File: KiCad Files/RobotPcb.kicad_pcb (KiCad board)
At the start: 2 copper layers, 68.8 x 98.6 mm, 35 parts, among them IC1 LM2576, IC2 LM2576, IC3 L293D, IC4 L293D, J1 Screw_Terminal_01x02, J10 Conn_01x03_Male, J11 Conn_01x03_Male, J2 Screw_Terminal_01x02, J3 Screw_Terminal_01x02, J4 Screw_Terminal_01x02, J5 Screw_Terminal_01x02, J6 Conn_01x16_Female, J7 Conn_01x16_Female, J8 Conn_01x03_Male, J9 Conn_01x03_Male

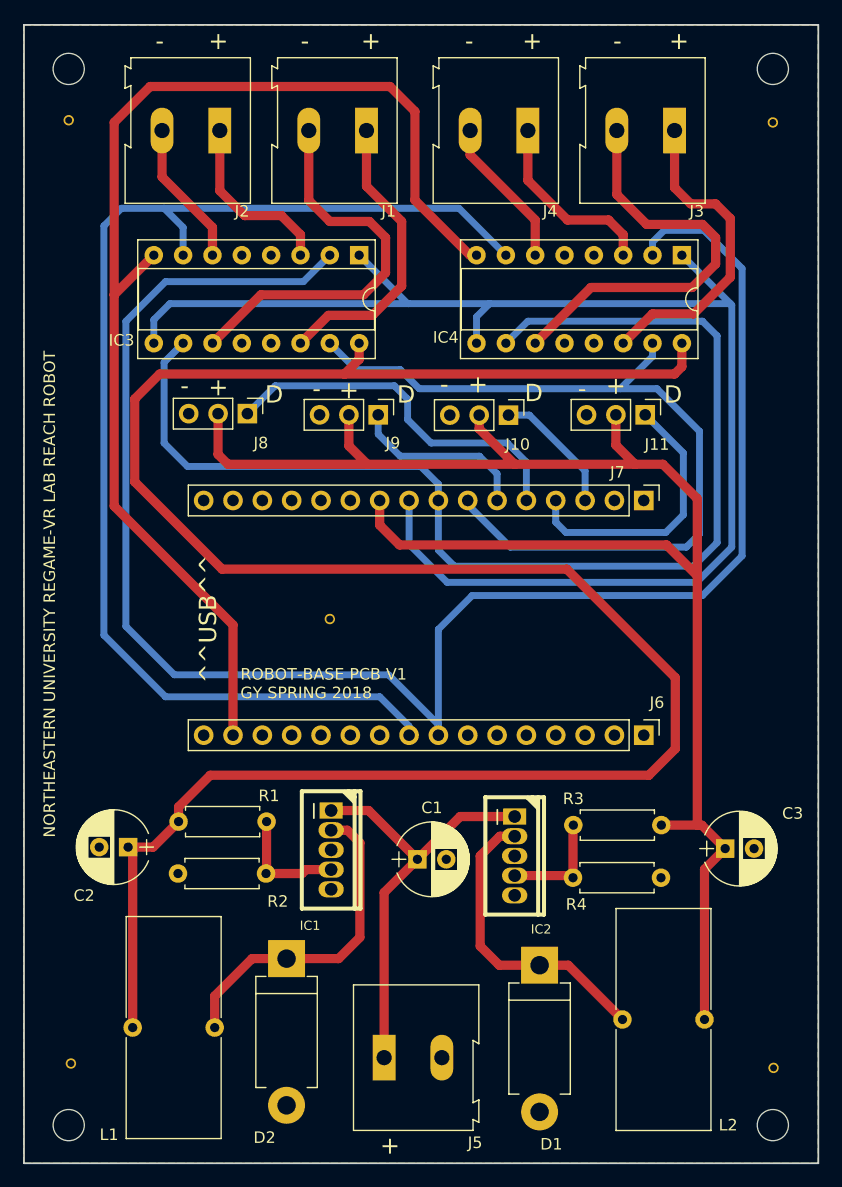
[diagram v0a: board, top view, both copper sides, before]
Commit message: Fixed PCBs
PCB v1.1

Added schematic PDF, updated pinout for PCB
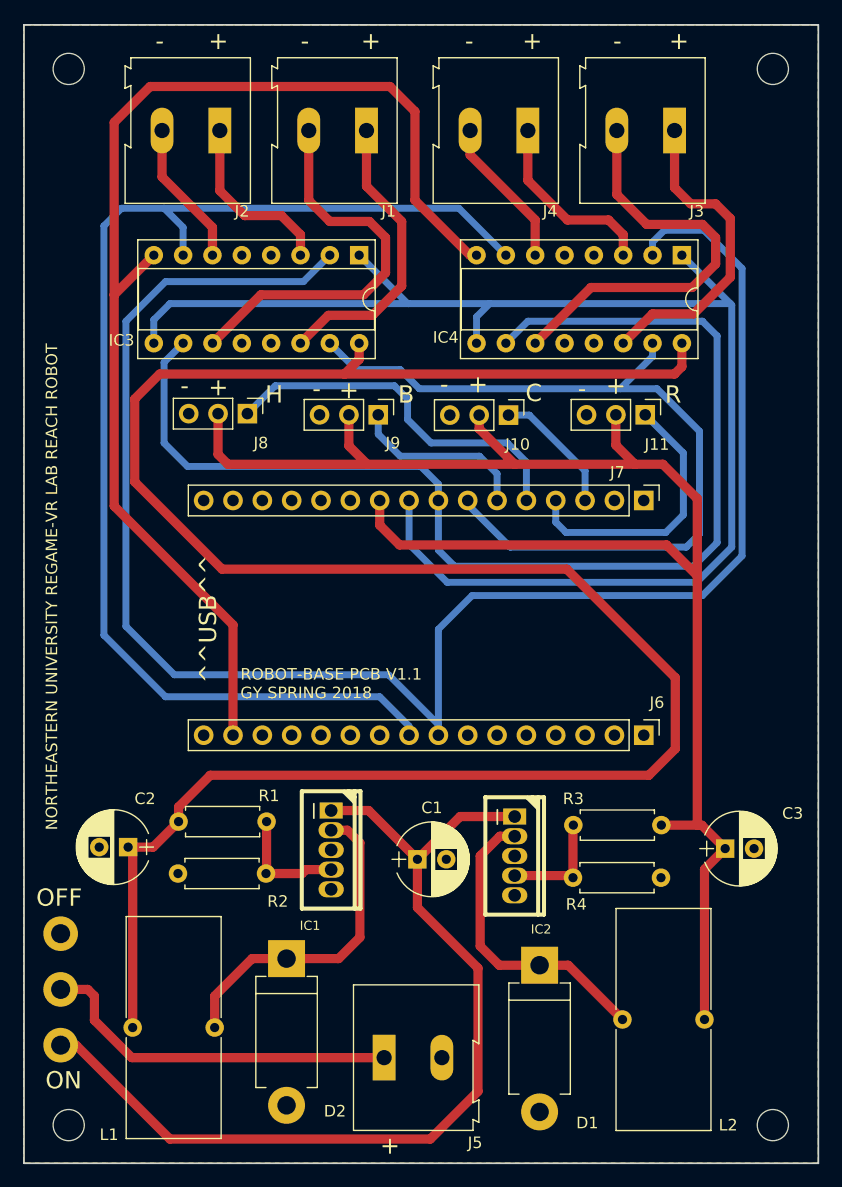
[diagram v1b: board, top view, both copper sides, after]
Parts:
- removed the REF** at (126.6, 87.4)
- removed the REF** at (104.2, 125.9)
- removed the REF** at (104.0, 44.2)
- removed the REF** at (165.0, 44.4)
- removed the REF** at (165.0, 126.2)
- added SW1: SW_SPDT, Custom footprints:L102021ML04Q_SPDT, F.Cu at (108.6, 119.4)
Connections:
- net SERVO_1_PWM renamed BASE_SERVO_PWM
- net SERVO_2_PWM renamed HEIGHT_SERVO_PWM
- net SERVO_3_PWM renamed REACH_SERVO_PWM
- net SERVO_4_PWM renamed CLAW_SERVO_PWM
- J5 pad 1: Net-(C1-Pad1) -> Net-(J5-Pad1)
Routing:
- net Net-(C1-Pad1): track 37.5 -> 82.6 mm
- net Net-(J5-Pad1): track 0.00 -> 31.7 mm
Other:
- board text added: "B"
- board text added: "C"
- board text added: "H"
- board text added: "OFF"
- board text added: "ON"
- board text added: "R"
- board text added: "ROBOT-BASE PCB V1.1 GY SPRING 2018"
- board text removed: "D"
- board text removed: "ROBOT-BASE PCB V1 GY SPRING 2018"
